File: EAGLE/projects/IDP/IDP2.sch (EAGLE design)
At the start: 8 parts, among them J1 22-05-7038-03, J2 22-05-7048-04, M1 IDP_PROTOBOARD, Q1 TEPT4400

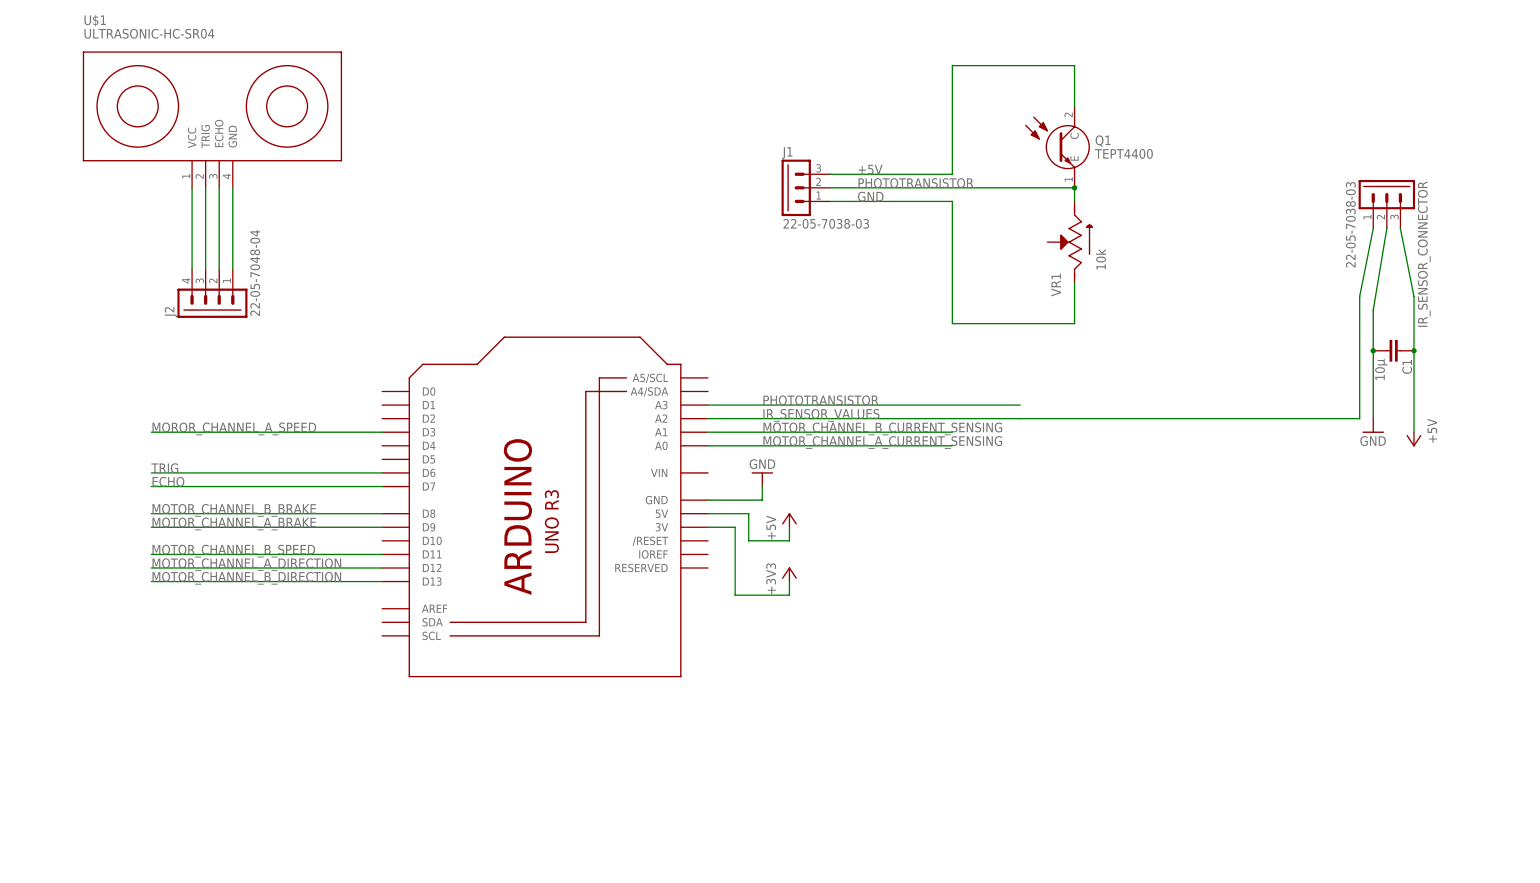
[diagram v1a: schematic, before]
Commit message: Include Servo and Change Phototransistor Layout
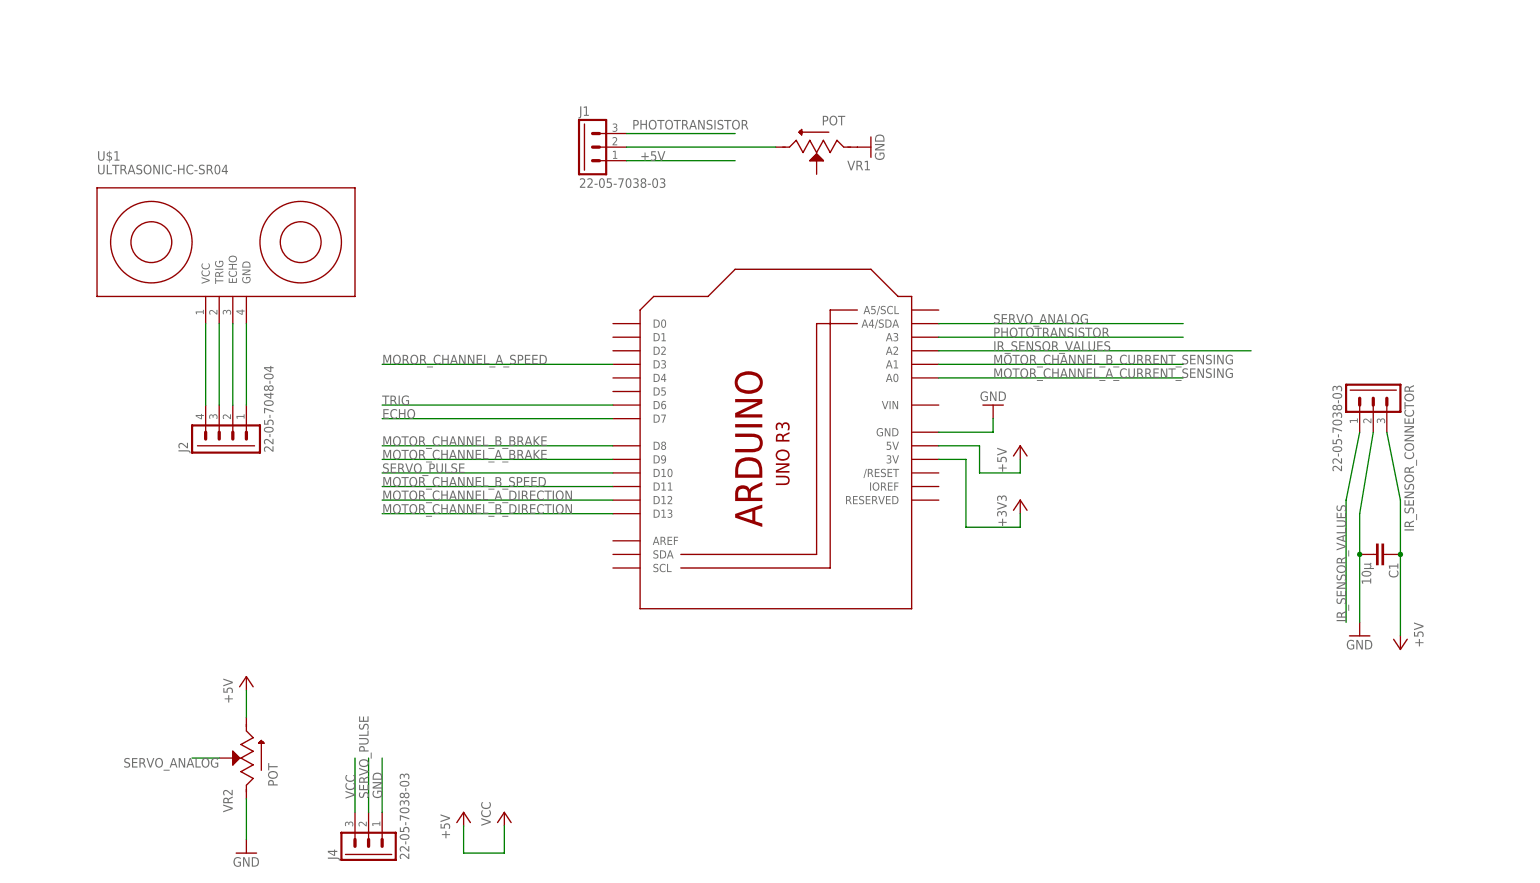
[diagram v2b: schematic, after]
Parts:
- removed Q1: TEPT4400, TEPT4400:TEPT4400
- added J4: 22-05-7038-03, IDP_library:22-05-7038-03
- added VR2: POT, IDP_library:POT
- VR1: value 10k -> POT
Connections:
- new net N$1: J1.2, VR1.CW
- new net SERVO_ANALOG: M1.A4/SDA, VR2.WIPER
- new net SERVO_PULSE: J4.2, M1.D10
- new net VCC: J4.3
- net +5V: now also J1.1, VR2.CW; no longer J1.3, Q1.C
- net GND: now also J4.1, VR2.CCW; no longer J1.1
- net PHOTOTRANSISTOR: now also J1.3; no longer J1.2, Q1.E, VR1.CW
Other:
- moved on the sheet: C1, IR_SENSOR_CONNECTOR, J1, J2, U$1, VR1

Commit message: Added Part Names
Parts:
- removed J2: 22-05-7048-04, IDP_library:22-05-7048-04
- removed U$1: ULTRASONIC-HC-SR04, diy-modules:ULTRASONIC-HC-SR04
- added ULTRASONIC_SENSOR: Rapid 22-1015/22-0915, IDP_library:22-05-7048-04
- IR_SENSOR_CONNECTOR, PHOTOTRANSISTOR, SERVO: value 22-05-7038-03 -> Rapid 22-1010 / 22-0910
- RAPID65-0753, RAPID68-1959: value POT -> 10K
- renumbered J1 to PHOTOTRANSISTOR, J4 to SERVO, VR1 to RAPID65-0753, VR2 to RAPID68-1959
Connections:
- net +5V: now also ULTRASONIC_SENSOR.4; no longer J2.4, U$1.VCC
- net ECHO: now also ULTRASONIC_SENSOR.2; no longer J2.2, U$1.ECHO
- net GND: now also ULTRASONIC_SENSOR.1; no longer J2.1, U$1.GND
- net TRIG: now also ULTRASONIC_SENSOR.3; no longer J2.3, U$1.TRIG
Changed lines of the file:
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@@
 <part name="+3V1" library="IDP_library" deviceset="+3V3" device=""/>
 <part name="GND1" library="IDP_library" deviceset="GND" device=""/>
-<part name="U$1" library="diy-modules" deviceset="ULTRASONIC-HC-SR04" device=""/>
-<part name="IR_SENSOR_CONNECTOR" library="IDP_library" deviceset="22-?-03" device="05-7038" package3d_urn="urn:adsk.eagle:package:8078646/1"/>
+<part name="IR_SENSOR_CONNECTOR" library="IDP_library" deviceset="22-?-03" device="05-7038" package3d_urn="urn:adsk.eagle:package:8078646/1" value="Rapid 22-1010 /  22-0910"/>
 <part name="C1" library="IDP_library" deviceset="C-EU" device="025-024X044" value="10μ"/>
 <part name="P+2" library="IDP_library" deviceset="+5V" device=""/>
 <part name="GND2" library="IDP_library" deviceset="GND" device=""/>
-<part name="J2" library="IDP_library" deviceset="22-?-04" device="05-7048" package3d_urn="urn:adsk.eagle:package:8078648/1" value="22-05-7048-04"/>
-<part name="J4" library="IDP_library" deviceset="22-?-03" device="05-7038" package3d_urn="urn:adsk.eagle:package:8078646/1"/>
+<part name="ULTRASONIC_SENSOR" library="IDP_library" deviceset="22-?-04" device="05-7048" package3d_urn="urn:adsk.eagle:package:8078648/1" value="Rapid 22-1015/22-0915"/>
+<part name="SERVO" library="IDP_library" deviceset="22-?-03" device="05-7038" package3d_urn="urn:adsk.eagle:package:8078646/1" value="Rapid 22-1010 /  22-0910"/>
 <part name="P+3" library="IDP_library" deviceset="+5V" device=""/>
 <part name="P+4" library="IDP_library" deviceset="VCC" device=""/>
-<part name="VR2" library="IDP_library" deviceset="POT" device=""/>
+<part name="RAPID68-1959" library="IDP_library" deviceset="POT" device="" value="10K"/>
 <part name="P+5" library="IDP_library" deviceset="+5V" device=""/>
 <part name="GND3" library="IDP_library" deviceset="GND" device=""/>
 <part name="GND4" library="IDP_library" deviceset="GND" device=""/>
-<part name="VR1" library="IDP_library" deviceset="POT" device=""/>
-<part name="J1" library="IDP_library" deviceset="22-?-03" device="05-7038" package3d_urn="urn:adsk.eagle:package:8078646/1"/>
+<part name="RAPID65-0753" library="IDP_library" deviceset="POT" device="" value="10K"/>
+<part name="PHOTOTRANSISTOR" library="IDP_library" deviceset="22-?-03" device="05-7038" package3d_urn="urn:adsk.eagle:package:8078646/1" value="Rapid 22-1010 /  22-0910"/>
 </parts>
 <sheets>
@@
 <attribute name="VALUE" x="226.06" y="93.98" size="1.778" layer="96" rot="R180"/>
 </instance>
-<instance part="U$1" gate="G$1" x="78.74" y="121.92" smashed="yes">
-<attribute name="NAME" x="55.88" y="137.16" size="1.778" layer="95"/>
-<attribute name="VALUE" x="55.88" y="134.62" size="1.778" layer="95"/>
-</instance>
 <instance part="IR_SENSOR_CONNECTOR" gate="G$1" x="294.64" y="93.98" smashed="yes" rot="R270">
-<attribute name="VALUE" x="287.02" y="95.25" size="1.778" layer="96" rot="R270"/>
-<attribute name="NAME" x="300.482" y="95.25" size="1.778" layer="95" rot="R270"/>
+<attribute name="VALUE" x="285.75" y="96.52" size="1.778" layer="96"/>
+<attribute name="NAME" x="283.21" y="99.822" size="1.778" layer="95"/>
 </instance>
 <instance part="C1" gate="G$1" x="297.18" y="63.5" smashed="yes" rot="R270">
@@
 <attribute name="VALUE" x="289.56" y="45.72" size="1.778" layer="96"/>
 </instance>
-<instance part="J2" gate="G$1" x="78.74" y="83.82" smashed="yes" rot="R90">
-<attribute name="VALUE" x="88.9" y="82.55" size="1.778" layer="96" rot="R90"/>
-<attribute name="NAME" x="72.898" y="82.55" size="1.778" layer="95" rot="R90"/>
-</instance>
-<instance part="J4" gate="G$1" x="106.68" y="7.62" smashed="yes" rot="R90">
+<instance part="ULTRASONIC_SENSOR" gate="G$1" x="71.12" y="86.36" smashed="yes">
+<attribute name="VALUE" x="74.93" y="76.2" size="1.778" layer="96" rot="R180"/>
+<attribute name="NAME" x="74.93" y="95.758" size="1.778" layer="95" rot="R180"/>
+</instance>
+<instance part="SERVO" gate="G$1" x="106.68" y="7.62" smashed="yes" rot="R90">
 <attribute name="VALUE" x="114.3" y="6.35" size="1.778" layer="96" rot="R90"/>
 <attribute name="NAME" x="100.838" y="6.35" size="1.778" layer="95" rot="R90"/>
@@
 <attribute name="VALUE" x="129.54" y="12.7" size="1.778" layer="96" rot="R90"/>
 </instance>
-<instance part="VR2" gate="G$1" x="83.82" y="25.4" smashed="yes" rot="R90">
-<attribute name="NAME" x="81.2658" y="15.232890625" size="1.784990625" layer="95" rot="R90"/>
+<instance part="RAPID68-1959" gate="G$1" x="83.82" y="25.4" smashed="yes" rot="R90">
+<attribute name="NAME" x="91.4258" y="17.772890625" size="1.784990625" layer="95" rot="R90"/>
 <attribute name="VALUE" x="89.674590625" y="20.053409375" size="1.7824" layer="96" rot="R90"/>
 </instance>
@@
 <attribute name="VALUE" x="203.2" y="137.16" size="1.778" layer="96" rot="R90"/>
 </instance>
-<instance part="VR1" gate="G$1" x="190.5" y="139.7" smashed="yes" rot="R180">
-<attribute name="NAME" x="200.667109375" y="137.1458" size="1.784990625" layer="95" rot="R180"/>
+<instance part="RAPID65-0753" gate="G$1" x="190.5" y="139.7" smashed="yes" rot="R180">
+<attribute name="NAME" x="198.127109375" y="134.6058" size="1.784990625" layer="95" rot="R180"/>
 <attribute name="VALUE" x="195.846590625" y="145.554590625" size="1.7824" layer="96" rot="R180"/>
 </instance>
-<instance part="J1" gate="G$1" x="147.32" y="139.7" smashed="yes">
-<attribute name="VALUE" x="146.05" y="132.08" size="1.778" layer="96"/>
-<attribute name="NAME" x="146.05" y="145.542" size="1.778" layer="95"/>
+<instance part="PHOTOTRANSISTOR" gate="G$1" x="147.32" y="139.7" smashed="yes">
+<attribute name="VALUE" x="128.27" y="132.08" size="1.778" layer="96"/>
+<attribute name="NAME" x="128.27" y="145.542" size="1.778" layer="95"/>
 </instance>
 </instances>
@@
 </segment>
 <segment>
-<pinref part="U$1" gate="G$1" pin="GND"/>
-<pinref part="J2" gate="G$1" pin="1"/>
-<wire x1="83.82" y1="91.44" x2="83.82" y2="106.68" width="0.1524" layer="91"/>
-</segment>
-<segment>
-<pinref part="J4" gate="G$1" pin="1"/>
+<pinref part="ULTRASONIC_SENSOR" gate="G$1" pin="1"/>
+<wire x1="78.74" y1="81.28" x2="93.98" y2="81.28" width="0.1524" layer="91"/>
+<label x="86.36" y="81.28" size="1.778" layer="95"/>
+</segment>
+<segment>
+<pinref part="SERVO" gate="G$1" pin="1"/>
 <wire x1="109.22" y1="15.24" x2="109.22" y2="25.4" width="0.1524" layer="91"/>
 <label x="109.22" y="17.78" size="1.778" layer="95" rot="R90"/>
 </segment>
 <segment>
-<pinref part="VR2" gate="G$1" pin="CCW"/>
+<pinref part="RAPID68-1959" gate="G$1" pin="CCW"/>
 <wire x1="83.82" y1="17.78" x2="83.82" y2="10.16" width="0.1524" layer="91"/>
 <pinref part="GND3" gate="1" pin="GND"/>
@@
 <segment>
 <pinref part="GND4" gate="1" pin="GND"/>
-<pinref part="VR1" gate="G$1" pin="CCW"/>
+<pinref part="RAPID65-0753" gate="G$1" pin="CCW"/>
 </segment>
 </net>
@@
 </segment>
 <segment>
-<pinref part="U$1" gate="G$1" pin="VCC"/>
-<pinref part="J2" gate="G$1" pin="4"/>
-<wire x1="76.2" y1="91.44" x2="76.2" y2="106.68" width="0.1524" layer="91"/>
+<pinref part="ULTRASONIC_SENSOR" gate="G$1" pin="4"/>
+<wire x1="78.74" y1="88.9" x2="93.98" y2="88.9" width="0.1524" layer="91"/>
+<label x="86.36" y="88.9" size="1.778" layer="95"/>
 </segment>
 <segment>
@@
 </segment>
 <segment>
-<pinref part="VR2" gate="G$1" pin="CW"/>
+<pinref part="RAPID68-1959" gate="G$1" pin="CW"/>
 <wire x1="83.82" y1="33.02" x2="83.82" y2="38.1" width="0.1524" layer="91"/>
 <pinref part="P+5" gate="1" pin="+5V"/>
 </segment>
 <segment>
-<pinref part="J1" gate="G$1" pin="1"/>
+<pinref part="PHOTOTRANSISTOR" gate="G$1" pin="1"/>
 <wire x1="154.94" y1="137.16" x2="175.26" y2="137.16" width="0.1524" layer="91"/>
 <label x="157.48" y="137.16" size="1.778" layer="95"/>
@@
 </segment>
 <segment>
-<pinref part="J1" gate="G$1" pin="3"/>
+<pinref part="PHOTOTRANSISTOR" gate="G$1" pin="3"/>
 <label x="177.8" y="144.78" size="1.778" layer="95" rot="R180"/>
 <wire x1="154.94" y1="142.24" x2="175.26" y2="142.24" width="0.1524" layer="91"/>
@@
 </segment>
 <segment>
-<pinref part="U$1" gate="G$1" pin="ECHO"/>
-<pinref part="J2" gate="G$1" pin="2"/>
-<wire x1="81.28" y1="91.44" x2="81.28" y2="106.68" width="0.1524" layer="91"/>
+<pinref part="ULTRASONIC_SENSOR" gate="G$1" pin="2"/>
+<wire x1="78.74" y1="83.82" x2="93.98" y2="83.82" width="0.1524" layer="91"/>
+<label x="86.36" y="83.82" size="1.778" layer="95"/>
 </segment>
 </net>
@@
 </segment>
 <segment>
-<pinref part="U$1" gate="G$1" pin="TRIG"/>
-<pinref part="J2" gate="G$1" pin="3"/>
-<wire x1="78.74" y1="91.44" x2="78.74" y2="106.68" width="0.1524" layer="91"/>
+<pinref part="ULTRASONIC_SENSOR" gate="G$1" pin="3"/>
+<wire x1="78.74" y1="86.36" x2="93.98" y2="86.36" width="0.1524" layer="91"/>
+<label x="86.36" y="86.36" size="1.778" layer="95"/>
 </segment>
 </net>
@@
 </segment>
 <segment>
-<pinref part="VR2" gate="G$1" pin="WIPER"/>
+<pinref part="RAPID68-1959" gate="G$1" pin="WIPER"/>
 <wire x1="78.74" y1="25.4" x2="73.66" y2="25.4" width="0.1524" layer="91"/>
 <label x="78.74" y="25.4" size="1.778" layer="95" rot="R180"/>
@@
 </segment>
 <segment>
-<pinref part="J4" gate="G$1" pin="2"/>
+<pinref part="SERVO" gate="G$1" pin="2"/>
 <wire x1="106.68" y1="15.24" x2="106.68" y2="25.4" width="0.1524" layer="91"/>
 <label x="106.68" y="17.78" size="1.778" layer="95" rot="R90"/>
@@
 <net name="VCC" class="0">
 <segment>
-<pinref part="J4" gate="G$1" pin="3"/>
+<pinref part="SERVO" gate="G$1" pin="3"/>
 <wire x1="104.14" y1="15.24" x2="104.14" y2="25.4" width="0.1524" layer="91"/>
 <label x="104.14" y="17.78" size="1.778" layer="95" rot="R90"/>
@@
 <net name="N$1" class="0">
 <segment>
-<pinref part="J1" gate="G$1" pin="2"/>
-<pinref part="VR1" gate="G$1" pin="CW"/>
+<pinref part="PHOTOTRANSISTOR" gate="G$1" pin="2"/>
+<pinref part="RAPID65-0753" gate="G$1" pin="CW"/>
 <wire x1="154.94" y1="139.7" x2="182.88" y2="139.7" width="0.1524" layer="91"/>
 </segment>
